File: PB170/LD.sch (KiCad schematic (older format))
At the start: 4 parts

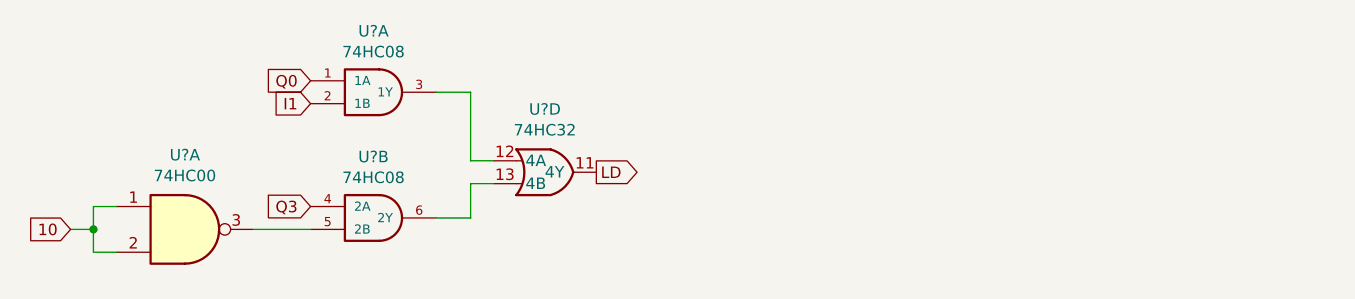
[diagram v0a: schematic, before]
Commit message: added LEDs, mby we could try to start routing
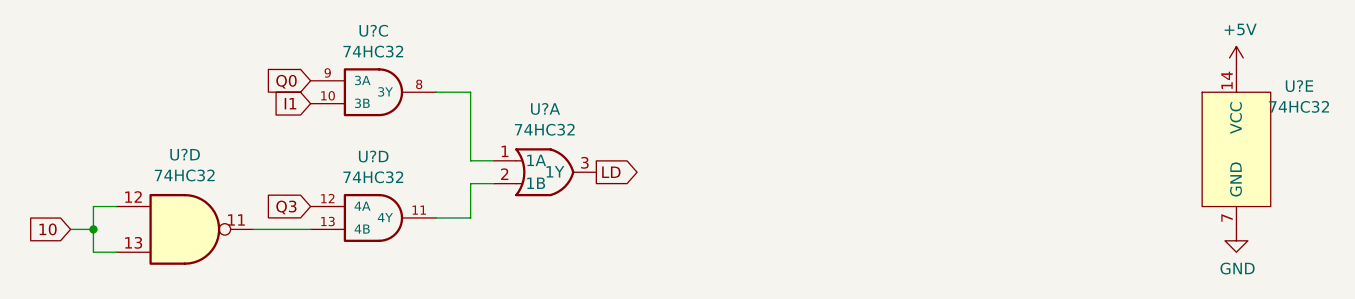
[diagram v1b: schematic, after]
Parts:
- added U?: 74HC32, Housings_SOIC:SOIC-14_3.9x8.7mm_Pitch1.27mm, symbol PB170:74HC32
- U? (x2): value 74HC08 -> 74HC32
- U?: value 74HC00 -> 74HC32; footprint Package_SO:TSSOP-14_4.4x5mm_P0.65mm -> Housings_SOIC:SOIC-14_3.9x8.7mm_Pitch1.27mm
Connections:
- net 10: now also U?.12, U?.13; no longer U?.1, U?.2
- net I1: now also U?.10 (3B); no longer U?.2 (1B)
- net LD: now also U?.3 (1Y); no longer U?.11 (4Y)
- net Q0: now also U?.9 (3A); no longer U?.1 (1A)
- net Q3: now also U?.12 (4A); no longer U?.4 (2A)
- new net: U?.1 (1A), U?.8 (3Y)
- new net: U?.11 (4Y), U?.2 (1B)
- new net: U?.11, U?.13 (4B)
- new net +5V: U?.14 (VCC)
- new net GND: U?.7 (GND)
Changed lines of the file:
@@
 $Comp
 L PB170:74HC32 U?
-U 4 1 6026CA63
+U 1 1 6026CA63
 P 6600 3850
 F 0 "U?" H 6575 4125 50  0000 C CNN
@@
 F 3 "https://datasheet.lcsc.com/szlcsc/Nexperia-74HC32D-653_C5632.pdf" H 6050 4050 50  0001 C CNN
 F 4 "C5632" H 6600 3850 50  0001 C CNN "LCSC"
-	4    6600 3850
+	1    6600 3850
 	1    0    0    -1
 $EndComp
 $Comp
 L PB170:74HC08 U?
-U 1 1 6026D84A
+U 3 1 6026D84A
 P 5800 3500
 F 0 "U?" H 5825 3767 50  0000 C CNN
-F 1 "74HC08" H 5825 3676 50  0000 C CNN
+F 1 "74HC32" H 5825 3676 50  0000 C CNN
 F 2 "Housings_SOIC:SOIC-14_3.9x8.7mm_Pitch1.27mm" H 5800 3500 50  0001 C CNN
-F 3 "https://datasheet.lcsc.com/szlcsc/Nexperia-74HC08D-653_C5593.pdf" H 5800 3500 50  0001 C CNN
+F 3 "https://datasheet.lcsc.com/szlcsc/Nexperia-74HC32D-653_C5632.pdf" H 5800 3500 50  0001 C CNN
 F 4 "C5593" H 5800 3500 50  0001 C CNN "LCSC"
-	1    5800 3500
+	3    5800 3500
 	1    0    0    -1
 $EndComp
 $Comp
 L PB170:74HC08 U?
-U 2 1 6026DC73
+U 4 1 6026DC73
 P 5800 4050
 F 0 "U?" H 5825 4317 50  0000 C CNN
-F 1 "74HC08" H 5825 4226 50  0000 C CNN
+F 1 "74HC32" H 5825 4226 50  0000 C CNN
 F 2 "Housings_SOIC:SOIC-14_3.9x8.7mm_Pitch1.27mm" H 5800 4050 50  0001 C CNN
-F 3 "https://datasheet.lcsc.com/szlcsc/Nexperia-74HC08D-653_C5593.pdf" H 5800 4050 50  0001 C CNN
+F 3 "https://datasheet.lcsc.com/szlcsc/Nexperia-74HC32D-653_C5632.pdf" H 5800 4050 50  0001 C CNN
 F 4 "C5593" H 5800 4050 50  0001 C CNN "LCSC"
-	2    5800 4050
+	4    5800 4050
 	1    0    0    -1
 $EndComp
@@
 $Comp
 L 74xx:74HC00 U?
-U 1 1 602AF9EC
+U 4 1 602AF9EC
 P 5000 4100
 F 0 "U?" H 5000 4425 50  0000 C CNN
-F 1 "74HC00" H 5000 4334 50  0000 C CNN
-F 2 "Package_SO:TSSOP-14_4.4x5mm_P0.65mm" H 5000 4100 50  0001 C CNN
-F 3 "https://datasheet.lcsc.com/szlcsc/Texas-Instruments-TI-SN74HC00PWR_C6807.pdf" H 5000 4100 50  0001 C CNN
+F 1 "74HC32" H 5000 4334 50  0000 C CNN
+F 2 "Housings_SOIC:SOIC-14_3.9x8.7mm_Pitch1.27mm" H 5000 4100 50  0001 C CNN
+F 3 "https://datasheet.lcsc.com/szlcsc/Nexperia-74HC32D-653_C5632.pdf" H 5000 4100 50  0001 C CNN
 F 4 "C6807" H 5000 4100 50  0001 C CNN "LCSC"
-	1    5000 4100
+	4    5000 4100
 	1    0    0    -1
 $EndComp
@@
 Text GLabel 4500 4100 0    50   Input ~ 0
 10
+$Comp
+L power:GND #PWR?
+U 1 1 602DD0AF
+P 9600 4100
+AR Path="/6026D736/602DD0AF" Ref="#PWR?"  Part="1"
+AR Path="/60270D42/602DD0AF" Ref="#PWR?"  Part="1"
+F 0 "#PWR?" H 9600 3850 50  0001 C CNN
+F 1 "GND" H 9605 3927 50  0000 C CNN
+F 2 "" H 9600 4100 50  0001 C CNN
+F 3 "" H 9600 4100 50  0001 C CNN
+	1    9600 4100
+	1    0    0    -1
+$EndComp
+$Comp
+L PB170:74HC32 U?
+U 5 1 602DD0B6
+P 9900 3750
+AR Path="/6026D736/602DD0B6" Ref="U?"  Part="5"
+AR Path="/60270D42/602DD0B6" Ref="U?"  Part="5"
+F 0 "U?" H 9875 4025 50  0000 C CNN
+F 1 "74HC32" H 9875 3934 50  0000 C CNN
+F 2 "Housings_SOIC:SOIC-14_3.9x8.7mm_Pitch1.27mm" H 9350 3950 50  0001 C CNN
+F 3 "https://datasheet.lcsc.com/szlcsc/Nexperia-74HC32D-653_C5632.pdf" H 9350 3950 50  0001 C CNN
+F 4 "C5632" H 9900 3750 50  0001 C CNN "LCSC"
+	5    9900 3750
+	1    0    0    -1
+$EndComp
+$Comp
+L power:+5V #PWR?
+U 1 1 602DD0BC
+P 9600 3400
+AR Path="/6026D736/602DD0BC" Ref="#PWR?"  Part="1"
+AR Path="/60270D42/602DD0BC" Ref="#PWR?"  Part="1"
+F 0 "#PWR?" H 9600 3250 50  0001 C CNN
+F 1 "+5V" H 9615 3573 50  0000 C CNN
+F 2 "" H 9600 3400 50  0001 C CNN
+F 3 "" H 9600 3400 50  0001 C CNN
+	1    9600 3400
+	1    0    0    -1
+$EndComp
 $EndSCHEMATC
